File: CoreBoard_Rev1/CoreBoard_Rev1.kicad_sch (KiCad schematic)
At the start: 16 parts, among them J1 RJ45_LED_Shielded, U1 OKI, U1 Teensy4.1_DEV-16771, U3 TSR_1-2450

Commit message: added buttons, lights, and a few other things from last year's board
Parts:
- added Conn4, Conn5, Conn6: Molex_SL_09, MRDT_Connectors:MOLEX_SL_09_Vertical, symbol MRDT_Connectors:Molex_SL_09
- added Conn7: Molex_SL_03, MRDT_Connectors:MOLEX_SL_03_Vertical, symbol MRDT_Connectors:Molex_SL_03
- added D10, D11, D12, D13, D14, D15, D16, D17, D18, D19, D20, D4, D5, D6, D7, D8, D9: BLUE, LED_SMD:LED_0603_1608Metric_Pad1.05x0.95mm_HandSolder, symbol Device:LED
- added D21: YELLOW, LED_SMD:LED_0603_1608Metric_Pad1.05x0.95mm_HandSolder, symbol Device:LED
- added R10, R11, R12, R13, R19, R20, R21, R22, R23, R29, R30, R31, R32, R33, R34, R9: 120, Resistor_SMD:R_0603_1608Metric_Pad0.98x0.95mm_HandSolder, symbol Device:R
- added R14, R15, R16, R17, R18, R24, R25, R26, R27, R28, R4, R5, R6, R7, R8: 4.7k, Resistor_SMD:R_0603_1608Metric_Pad0.98x0.95mm_HandSolder, symbol Device:R
- added R35: 100, Resistor_SMD:R_0603_1608Metric_Pad0.98x0.95mm_HandSolder, symbol Device:R
- added R36: 300, Resistor_SMD:R_0603_1608Metric_Pad0.98x0.95mm_HandSolder, symbol Device:R
- added SW1, SW10, SW11, SW12, SW13, SW14, SW15, SW2, SW3, SW4, SW5, SW6, SW7, SW8, SW9: SW_Push, Button_Switch_SMD:SW_SPST_TL3305A, symbol Switch:SW_Push
- added SW16: SW_SPDT, Button_Switch_THT:SW_Slide_1P2T_CK_OS102011MS2Q, symbol Switch:SW_SPDT
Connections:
- net +3V3: now also D10.2 (A), D11.2 (A), D12.2 (A), D13.2 (A), D14.2 (A), D15.2 (A), D16.2 (A), D17.2 (A), D18.2 (A), D4.2 (A), D5.2 (A), D6.2 (A), D7.2 (A), D8.2 (A), D9.2 (A), R14.1, R15.1, R16.1, R17.1, R18.1, R24.1, R25.1, R26.1, R27.1, R28.1, R4.1, R5.1, R6.1, R7.1, R8.1, SW16.3 (C)
- net +5V: now also Conn4.2, Conn4.5, Conn4.8, Conn5.2, Conn5.5, Conn5.8, Conn6.2, Conn6.5, Conn6.8
- net GND: now also Conn4.1, Conn4.4, Conn4.7, Conn5.1, Conn5.4, Conn5.7, Conn6.1, Conn6.4, Conn6.7, Conn7.2, D19.1 (K), D20.1 (K), D21.1 (K), SW1.1, SW10.1, SW11.1, SW12.1, SW13.1, SW14.1, SW15.1, SW16.1 (A), SW2.1, SW3.1, SW4.1, SW5.1, SW6.1, SW7.1, SW8.1, SW9.1
- net MR_TX: now also U1.20 (A6); no longer U1.22 (A8)
- net NeoPixels: now reaches U1.11 (MOSI)
- net NeoPixels: now also Conn7.3
- net ServoPWM7: now reaches U1.12 (MISO)
- net ServoPWM7: now also Conn6.3
- net ServoPWM9: now reaches U1.18 (A4)
- net ServoPWM9: now also Conn6.9
- net ServoPWM8: now reaches U1.19 (A5)
- net ServoPWM8: now also Conn6.6
- net ServoPWM4: now reaches U1.2 (OUT2)
- net ServoPWM4: now also Conn5.9
- net LEDRX: now reaches U1.23 (A9)
- net LEDRX: now also R36.1
- net ServoPWM1: now reaches U1.3 (LRCLK2)
- net ServoPWM1: now also Conn4.9
- net ServoPWM3: now reaches U1.33 (MCLK2)
- net ServoPWM3: now also Conn4.3
- net ServoPWM2: now reaches U1.4 (BCLK2)
- net ServoPWM2: now also Conn4.6
- net REVERSE: now reaches U1.5 (IN2)
- net REVERSE: now also R34.2, SW16.2 (B)
- net ServoPWM5: now reaches U1.6 (OUT1D)
- net ServoPWM5: now also U1.9 (OUT1C), Conn5.3, Conn5.6
- new net: D8.1 (K), R13.2
- new net: D6.1 (K), R11.2
- new net: D9.1 (K), R19.2
- new net: D10.1 (K), R20.2
- new net: D17.1 (K), R32.2
- new net: D19.2 (A), R34.1
- new net: D13.1 (K), R23.2
- new net: D5.1 (K), R10.2
- new net: D21.2 (A), R36.2
- new net: D4.1 (K), R9.2
- new net: D20.2 (A), R35.2
- new net: D12.1 (K), R22.2
- new net: D14.1 (K), R29.2
- new net: D18.1 (K), R33.2
- new net: D15.1 (K), R30.2
- new net: D16.1 (K), R31.2
- new net: D7.1 (K), R12.2
- new net: D11.1 (K), R21.2
- new net +5VA: Conn7.1
- new net B1: R4.2, R9.1, SW1.2
- new net B10: R12.1, R7.2, SW4.2
- new net B11: R17.2, R22.1, SW9.2
- new net B12: R27.2, R32.1, SW14.2
- new net B13: R13.1, R8.2, SW5.2
- new net B14: R18.2, R23.1, SW10.2
- new net B15: R28.2, R33.1, SW15.2
- new net B2: R14.2, R19.1, SW6.2
- new net B3: R24.2, R29.1, SW11.2
- new net B4: R10.1, R5.2, SW2.2
- new net B5: R15.2, R20.1, SW7.2
- new net B6: R25.2, R30.1, SW12.2
- new net B7: R11.1, R6.2, SW3.2
- new net B8: R16.2, R21.1, SW8.2
- new net B9: R26.2, R31.1, SW13.2
- new net LEDTX: R35.1, U1.22 (A8)
- no-connect marks 7 -> 6
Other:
- moved on the sheet: C1, J1

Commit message: Changes to Schematic
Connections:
- net +5VA is gone; now on net +5V: Conn7.1
- net REVERSE renamed ReverseSW
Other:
- moved on the sheet: Conn7, D1, D10, D11, D12, D13, D14, D15, D16, D17, D18, D19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

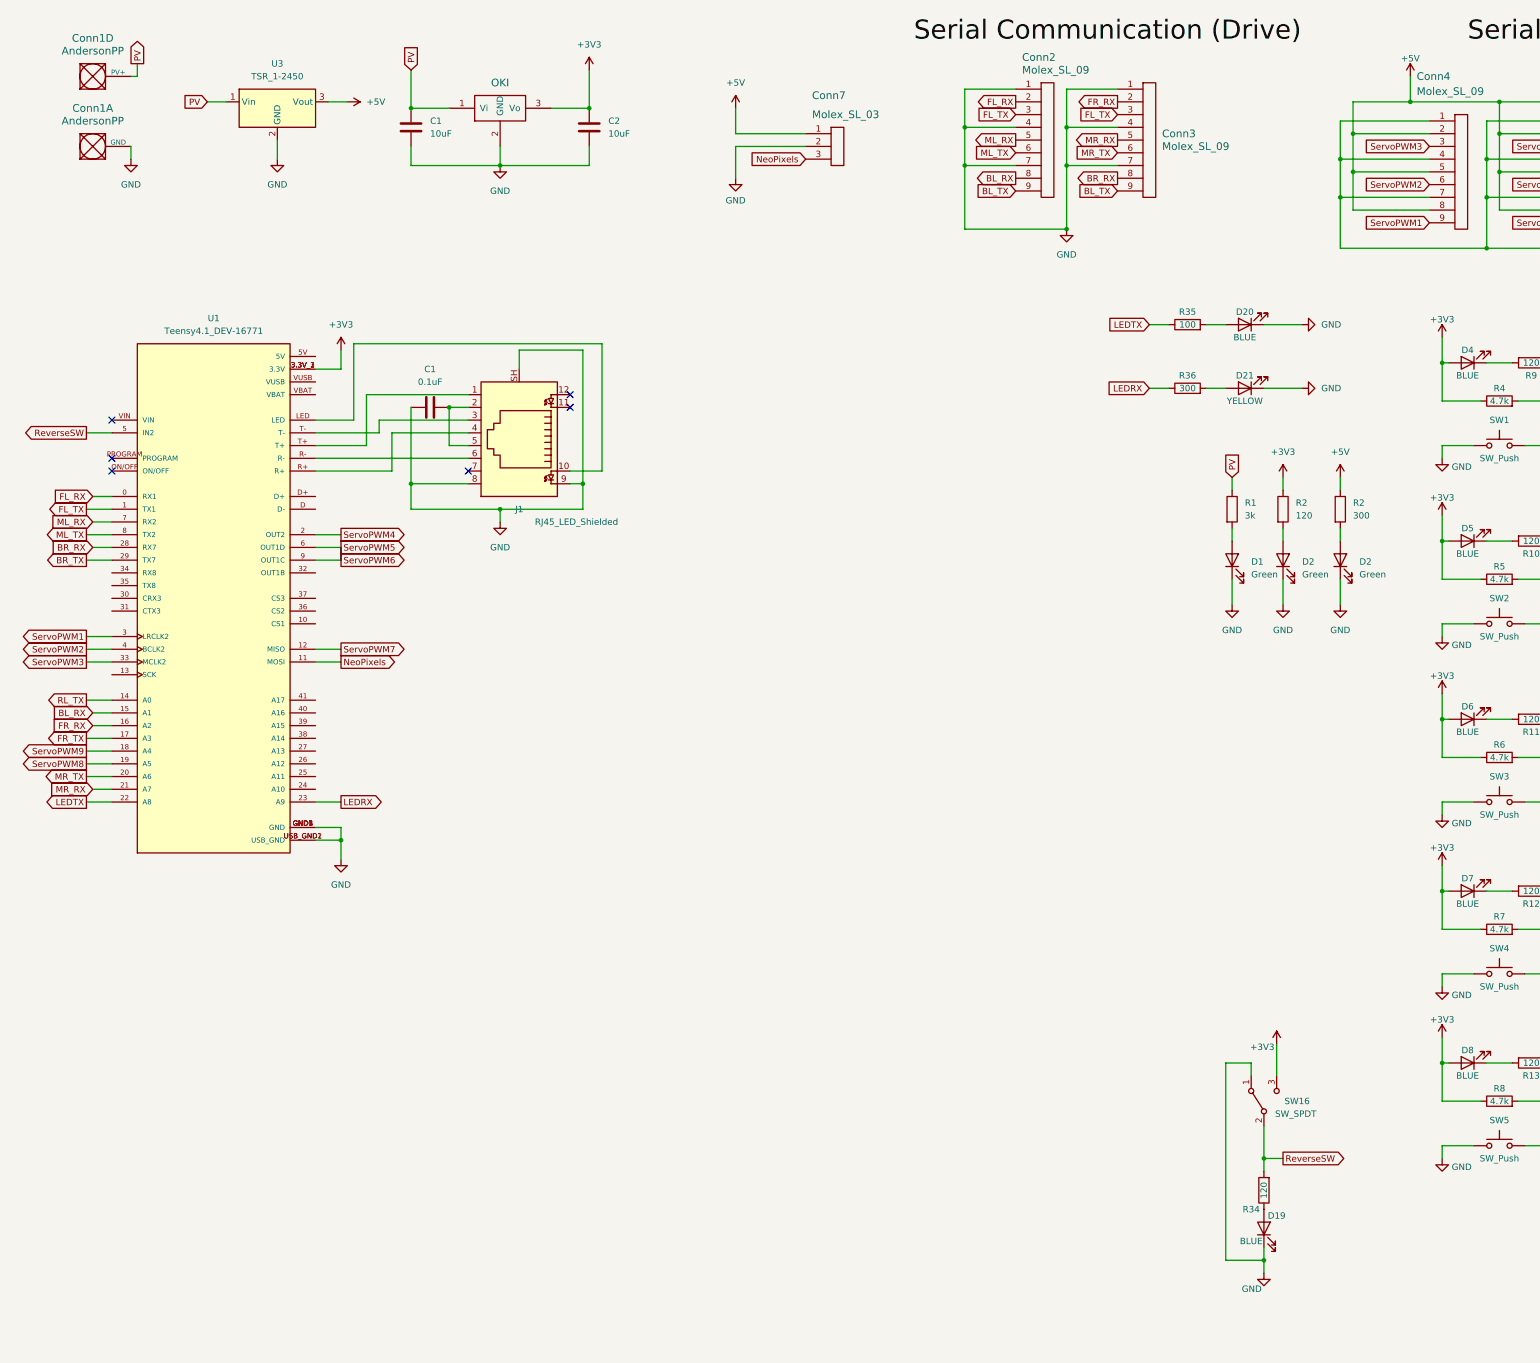
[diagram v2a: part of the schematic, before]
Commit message: figured out buttons, deleted some leds
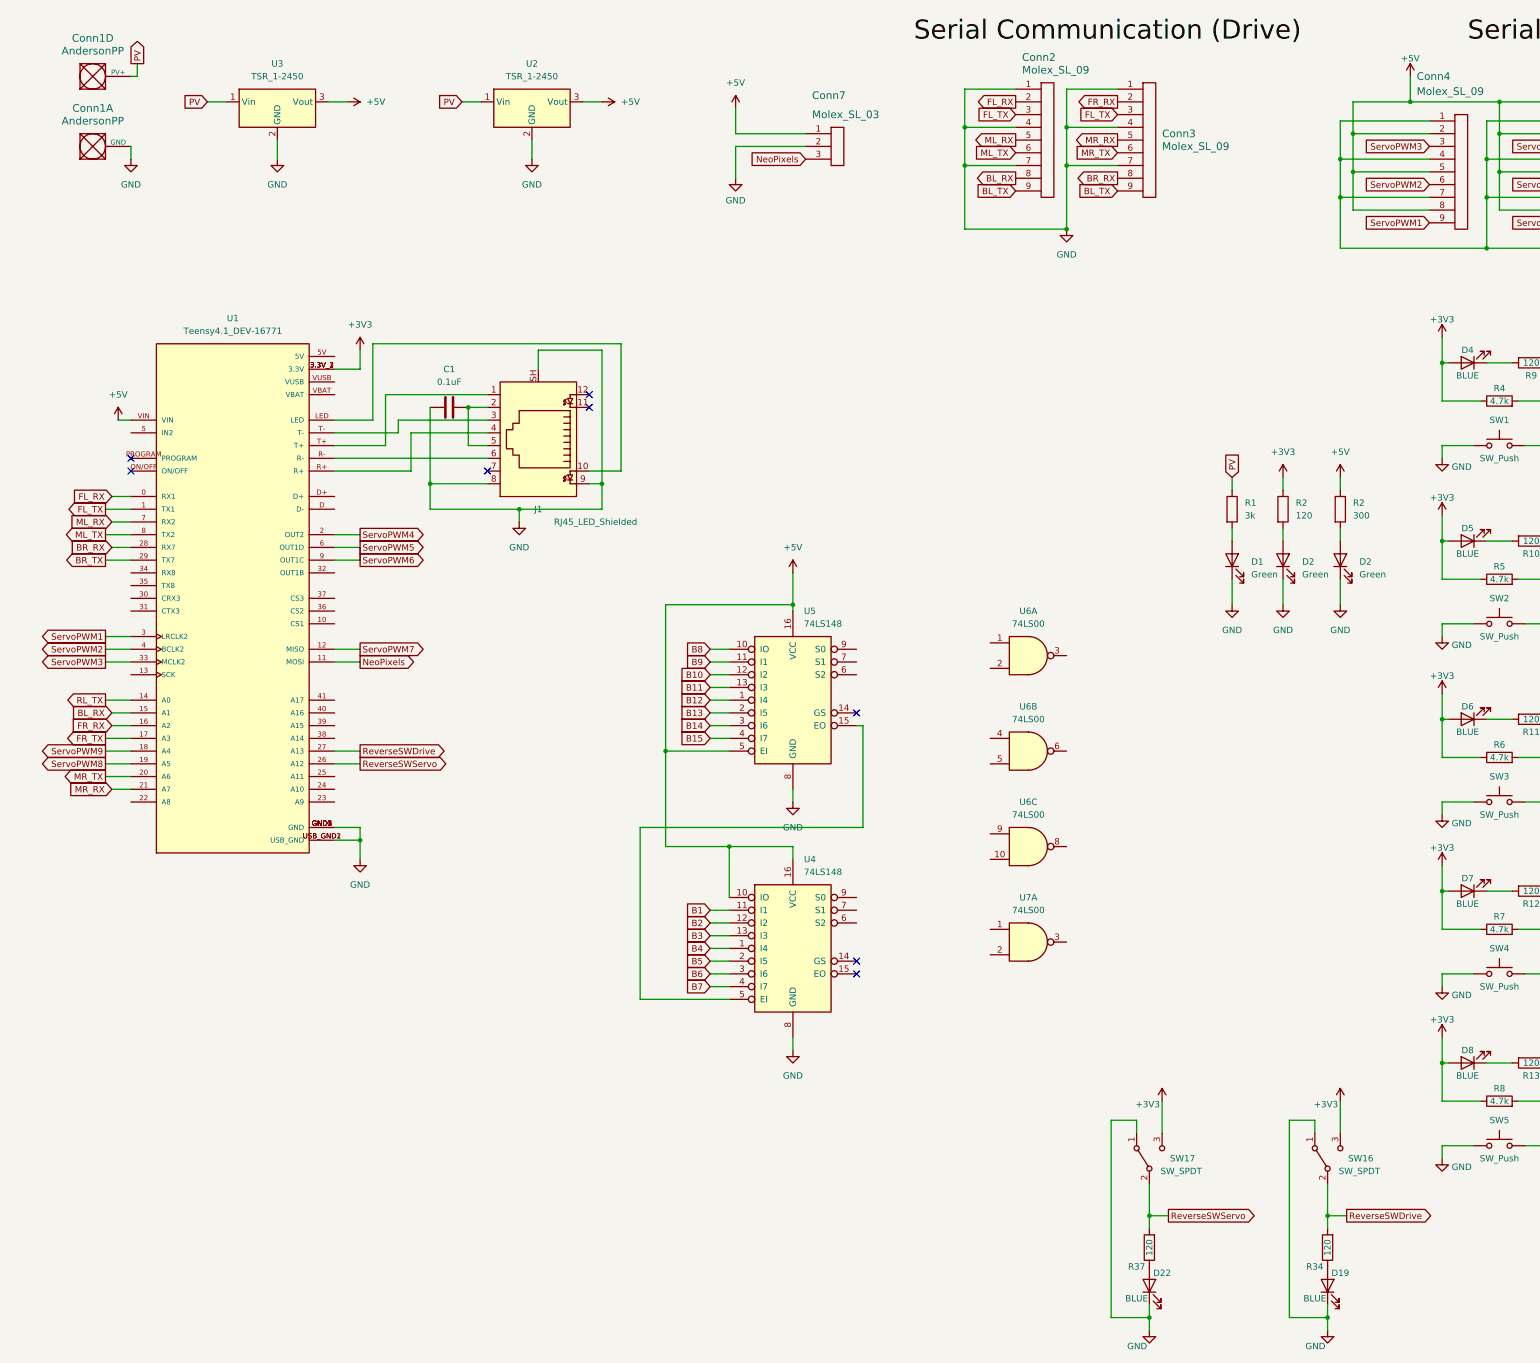
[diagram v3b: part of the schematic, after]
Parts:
- removed C1, C2: 10uF, Capacitor_SMD:C_0603_1608Metric_Pad1.08x0.95mm_HandSolder, symbol Device:C
- removed D20: BLUE, LED_SMD:LED_0603_1608Metric_Pad1.05x0.95mm_HandSolder, symbol Device:LED
- removed D21: YELLOW, LED_SMD:LED_0603_1608Metric_Pad1.05x0.95mm_HandSolder, symbol Device:LED
- removed R35: 100, Resistor_SMD:R_0603_1608Metric_Pad0.98x0.95mm_HandSolder, symbol Device:R
- removed R36: 300, Resistor_SMD:R_0603_1608Metric_Pad0.98x0.95mm_HandSolder, symbol Device:R
- removed U1: OKI, MRDT_Devices:OKI_Horizontal, symbol MRDT_Devices:OKI
- added D22: BLUE, LED_SMD:LED_0603_1608Metric_Pad1.05x0.95mm_HandSolder, symbol Device:LED
- added R37: 120, Resistor_SMD:R_0603_1608Metric_Pad0.98x0.95mm_HandSolder, symbol Device:R
- added SW17: SW_SPDT, Button_Switch_THT:SW_Slide_1P2T_CK_OS102011MS2Q, symbol Switch:SW_SPDT
- added U2: TSR_1-2450, Converter_DCDC:Converter_DCDC_TRACO_TSR-1_THT, symbol Regulator_Switching:TSR_1-2450
- added U4, U5: 74LS148, symbol 74xx:74LS148
- added U6, U7: 74LS00, symbol 74xx:74LS00
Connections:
- net +3V3: now also SW17.3 (C)
- net +5V: now also U1.VIN, U2.3 (Vout), U4.10 (IO), U4.16 (VCC), U5.16 (VCC), U5.5 (EI)
- net B1: now also U4.11 (I1)
- net B10: now also U5.12 (I2)
- net B11: now also U5.13 (I3)
- net B12: now also U5.1 (I4)
- net B13: now also U5.2 (I5)
- net B14: now also U5.3 (I6)
- net B15: now also U5.4 (I7)
- net B2: now also U4.12 (I2)
- net B3: now also U4.13 (I3)
- net B4: now also U4.1 (I4)
- net B5: now also U4.2 (I5)
- net B6: now also U4.3 (I6)
- net B7: now also U4.4 (I7)
- net B8: now also U5.10 (IO)
- net B9: now also U5.11 (I1)
- net GND: now also D22.1 (K), SW17.1 (A), U2.2 (GND), U4.8 (GND), U5.8 (GND)
- net PV: now also U2.1 (Vin)
- net ReverseSWServo: now reaches U1.26 (A12)
- net ReverseSWServo: now also R37.2, SW17.2 (B)
- net ReverseSWDrive: now reaches U1.27 (A13)
- net ReverseSWDrive: now also R34.2, SW16.2 (B)
- net LEDRX: no longer names the net of U1.23 (A9)
- net LEDTX: no longer names the net of U1.22 (A8)
- removed net ReverseSW: R34.2, SW16.2 (B), U1.5 (IN2)
- new net: D22.2 (A), R37.1
- new net: U4.5 (EI), U5.15 (EO)
- no-connect marks 6 -> 8
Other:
- moved on the sheet: C1, D19, J1, R34, SW16, U1
